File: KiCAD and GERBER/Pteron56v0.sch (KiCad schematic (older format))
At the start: 46 parts, among them J1 AudioJack4, J2 AudioJack4, SW10 SW_PUSH, SW12 SW_PUSH, SW13 SW_PUSH, SW14 SW_PUSH, SW15 SW_PUSH, SW17 SW_PUSH, SW18 SW_PUSH, SW19 SW_PUSH, SW20 SW_PUSH, SW22 SW_PUSH, SW23 SW_PUSH, SW24 SW_PUSH, SW26 SW_PUSH, SW27 SW_PUSH, SW28 SW_PUSH, SW7 SW_PUSH, SW8 SW_PUSH, SW9 SW_PUSH, U1 ProMicro

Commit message: simplified wiring, lily58 like pro micro placement
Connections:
- net Col1: now also U1.17 (F7); no longer U1.13 (B6)
- net Col2: now also U1.16 (B1); no longer U1.15 (B3)
- net Col3: now also U1.15 (B3); no longer U1.16 (B1)
- net Col4: now also U1.14 (B2); no longer U1.18 (F6)
- net Col5: now also U1.13 (B6); no longer U1.17 (F7)
- net Row1: now also U1.10 (E6); no longer U1.9 (D7)
- net Row2: now also U1.9 (D7); no longer U1.10 (E6)
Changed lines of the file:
@@
 Text Label 3350 4000 0    50   ~ 0
 Col4
+Text Label 8100 5450 0    50   ~ 0
+Row1
 Text Label 8100 5350 0    50   ~ 0
-Row1
-Text Label 8100 5450 0    50   ~ 0
 Row2
 Text Label 8100 5550 0    50   ~ 0
@@
 Text Label 8100 5650 0    50   ~ 0
 Row4
-Text Label 10000 5650 0    50   ~ 0
+Text Label 10000 5250 0    50   ~ 0
 Col1
+Text Label 10000 5350 0    50   ~ 0
+Col2
 Text Label 10000 5450 0    50   ~ 0
-Col2
-Text Label 10000 5350 0    50   ~ 0
 Col3
-Text Label 10000 5150 0    50   ~ 0
+Text Label 10000 5550 0    50   ~ 0
 Col4
-Text Label 10000 5250 0    50   ~ 0
-Col5
 Wire Wire Line
 	8100 5650 8400 5650
 Wire Wire Line
-	9800 5150 10000 5150
-Wire Wire Line
 	9800 5250 10000 5250
 Wire Wire Line
 	9800 5350 10000 5350
-Wire Wire Line
-	9800 5450 10000 5450
 Wire Wire Line
 	9800 5650 10000 5650
@@
 	1    0    0    -1
 $EndComp
+Wire Wire Line
+	9800 5550 10000 5550
+Wire Wire Line
+	9800 5450 10000 5450
+Text Label 10000 5650 0    50   ~ 0
+Col5
 $EndSCHEMATC

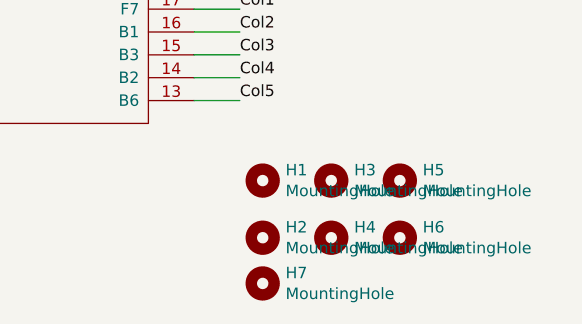
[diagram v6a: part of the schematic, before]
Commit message: made small changes for mounting holes
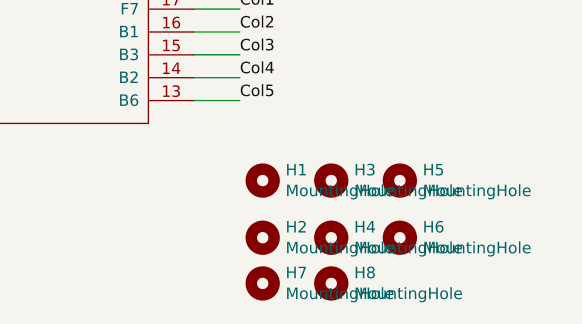
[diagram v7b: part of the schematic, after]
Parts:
- added H8: MountingHole, MountingHole:MountingHole_3.2mm_M3, symbol Mechanical:MountingHole
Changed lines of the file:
@@
 Text Label 10000 5650 0    50   ~ 0
 Col5
+$Comp
+L Mechanical:MountingHole H8
+U 1 1 60793C0F
+P 10400 6450
+F 0 "H8" H 10500 6496 50  0000 L CNN
+F 1 "MountingHole" H 10500 6405 50  0000 L CNN
+F 2 "MountingHole:MountingHole_3.2mm_M3" H 10400 6450 50  0001 C CNN
+F 3 "~" H 10400 6450 50  0001 C CNN
+	1    10400 6450
+	1    0    0    -1
+$EndComp
 $EndSCHEMATC

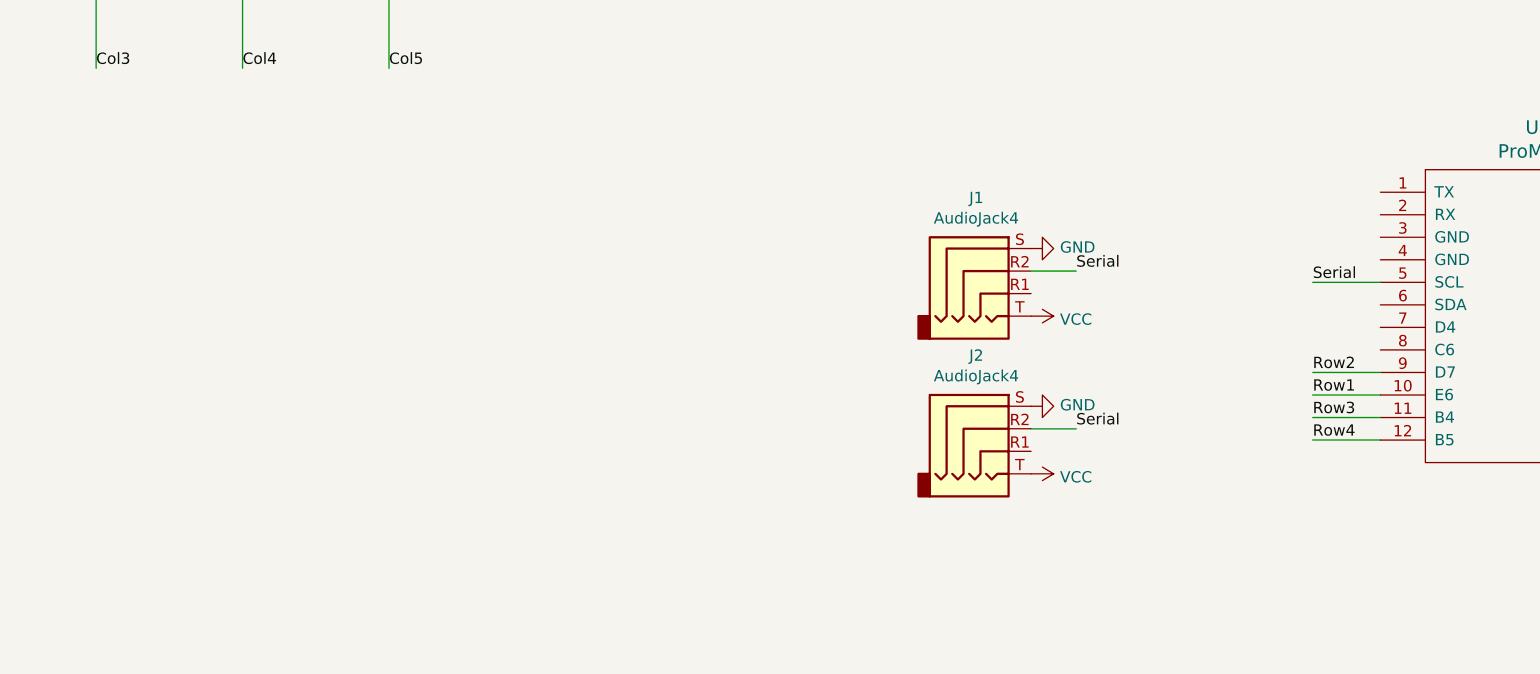
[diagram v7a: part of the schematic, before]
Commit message: added oled support
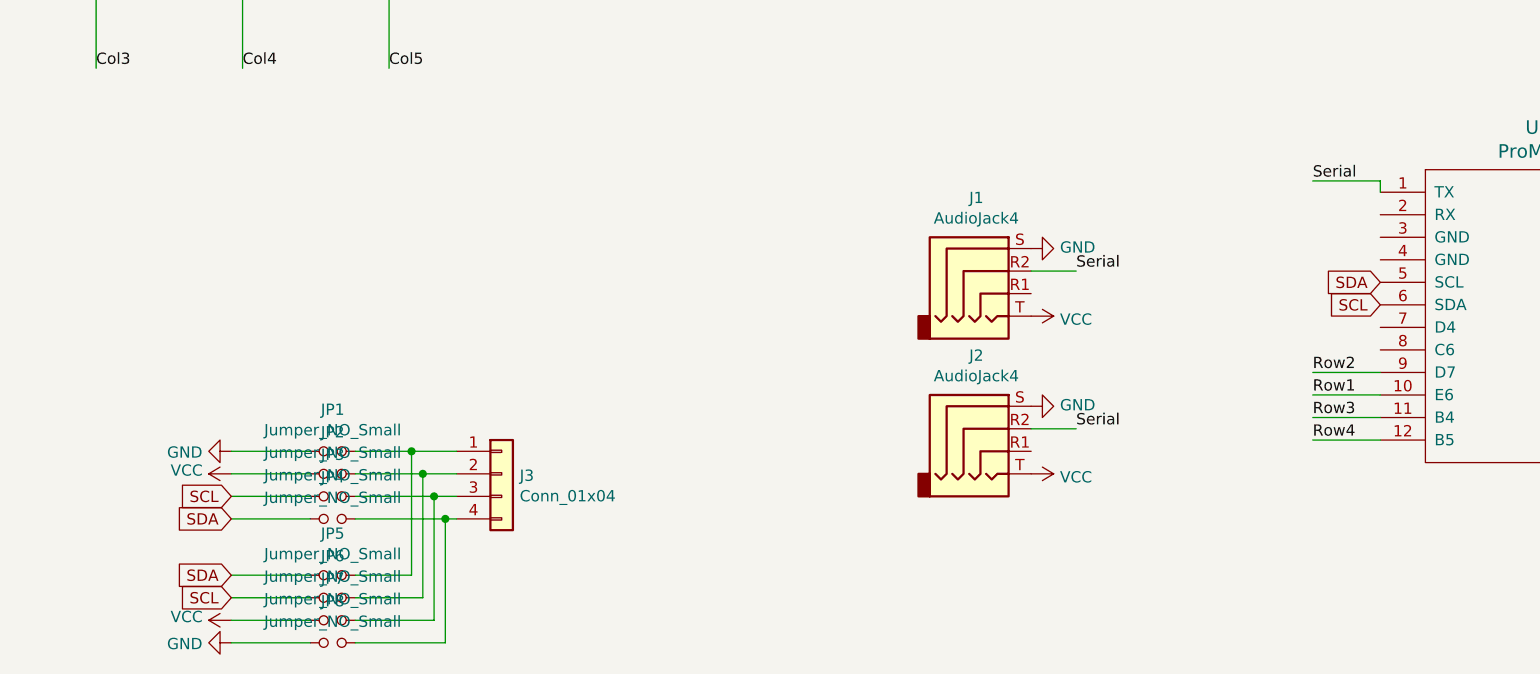
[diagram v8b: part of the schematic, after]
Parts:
- added J3: Conn_01x04, usbc_footprint:OLED_4Pin_outline, symbol Connector_Generic:Conn_01x04
- added JP1, JP2, JP3, JP4, JP5, JP6, JP7, JP8: Jumper_NO_Small, SparkFun-Passives:PAD-JUMPER-2-NO_NO_SILK, symbol Device:Jumper_NO_Small
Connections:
- net GND: now also JP1.1, JP8.1
- net Serial: now also U1.1 (TX); no longer U1.5 (SCL)
- net VCC: now also JP2.1, JP7.1
- net SCL: now reaches U1.6 (SDA)
- net SCL: now also JP3.1, JP6.1
- new net: J3.1 (Pin_1), JP1.2, JP5.2
- new net: J3.2 (Pin_2), JP2.2, JP6.2
- new net: J3.3 (Pin_3), JP3.2, JP7.2
- new net: J3.4 (Pin_4), JP4.2, JP8.2
- new net SDA: JP4.1, JP5.1, U1.5 (SCL)
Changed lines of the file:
@@
 Wire Wire Line
 	8100 5550 8400 5550
-Wire Wire Line
-	8400 4950 8100 4950
-Text Label 8100 4950 0    50   ~ 0
+Text Label 8100 4500 0    50   ~ 0
 Serial
 $Comp
@@
 	1    0    0    -1
 $EndComp
+$Comp
+L Connector_Generic:Conn_01x04 J3
+U 1 1 60775285
+P 4500 5800
+F 0 "J3" H 4580 5792 50  0000 L CNN
+F 1 "Conn_01x04" H 4580 5701 50  0000 L CNN
+F 2 "usbc_footprint:OLED_4Pin_outline" H 4500 5800 50  0001 C CNN
+F 3 "~" H 4500 5800 50  0001 C CNN
+	1    4500 5800
+	1    0    0    -1
+$EndComp
+Wire Wire Line
+	8100 4500 8400 4500
+Wire Wire Line
+	8400 4500 8400 4550
+Wire Wire Line
+	4300 5700 4100 5700
+Wire Wire Line
+	4300 5800 4150 5800
+Wire Wire Line
+	3850 5900 4200 5900
+Wire Wire Line
+	4300 6000 4250 6000
+Wire Wire Line
+	4100 5700 4100 6250
+Wire Wire Line
+	4100 6250 3850 6250
+Connection ~ 4100 5700
+Wire Wire Line
+	4100 5700 3850 5700
+Wire Wire Line
+	4150 5800 4150 6350
+Wire Wire Line
+	4150 6350 3850 6350
+Connection ~ 4150 5800
+Wire Wire Line
+	4150 5800 3850 5800
+Wire Wire Line
+	4200 5900 4200 6450
+Wire Wire Line
+	4200 6450 3850 6450
+Connection ~ 4200 5900
+Wire Wire Line
+	4200 5900 4300 5900
+Wire Wire Line
+	4250 6000 4250 6550
+Wire Wire Line
+	4250 6550 3850 6550
+Connection ~ 4250 6000
+Wire Wire Line
+	4250 6000 3850 6000
+$Comp
+L Device:Jumper_NO_Small JP1
+U 1 1 60791352
+P 3750 5700
+F 0 "JP1" H 3750 5885 50  0000 C CNN
+F 1 "Jumper_NO_Small" H 3750 5794 50  0000 C CNN
+F 2 "SparkFun-Passives:PAD-JUMPER-2-NO_NO_SILK" H 3750 5700 50  0001 C CNN
+F 3 "~" H 3750 5700 50  0001 C CNN
+	1    3750 5700
+	1    0    0    -1
+$EndComp
+$Comp
+L Device:Jumper_NO_Small JP2
+U 1 1 607919BE
+P 3750 5800
+F 0 "JP2" H 3750 5985 50  0000 C CNN
+F 1 "Jumper_NO_Small" H 3750 5894 50  0000 C CNN
+F 2 "SparkFun-Passives:PAD-JUMPER-2-NO_NO_SILK" H 3750 5800 50  0001 C CNN
+F 3 "~" H 3750 5800 50  0001 C CNN
+	1    3750 5800
+	1    0    0    -1
+$EndComp
+$Comp
+L Device:Jumper_NO_Small JP3
+U 1 1 60791C36
+P 3750 5900
+F 0 "JP3" H 3750 6085 50  0000 C CNN
+F 1 "Jumper_NO_Small" H 3750 5994 50  0000 C CNN
+F 2 "SparkFun-Passives:PAD-JUMPER-2-NO_NO_SILK" H 3750 5900 50  0001 C CNN
+F 3 "~" H 3750 5900 50  0001 C CNN
+	1    3750 5900
+	1    0    0    -1
+$EndComp
+$Comp
+L Device:Jumper_NO_Small JP4
+U 1 1 60791EC7
+P 3750 6000
+F 0 "JP4" H 3750 6185 50  0000 C CNN
+F 1 "Jumper_NO_Small" H 3750 6094 50  0000 C CNN
+F 2 "SparkFun-Passives:PAD-JUMPER-2-NO_NO_SILK" H 3750 6000 50  0001 C CNN
+F 3 "~" H 3750 6000 50  0001 C CNN
+	1    3750 6000
+	1    0    0    -1
+$EndComp
+$Comp
+L Device:Jumper_NO_Small JP5
+U 1 1 60792104
+P 3750 6250
+F 0 "JP5" H 3750 6435 50  0000 C CNN
+F 1 "Jumper_NO_Small" H 3750 6344 50  0000 C CNN
+F 2 "SparkFun-Passives:PAD-JUMPER-2-NO_NO_SILK" H 3750 6250 50  0001 C CNN
+F 3 "~" H 3750 6250 50  0001 C CNN
+	1    3750 6250
+	1    0    0    -1
+$EndComp
+$Comp
+L Device:Jumper_NO_Small JP6
+U 1 1 607923D2
+P 3750 6350
+F 0 "JP6" H 3750 6535 50  0000 C CNN
+F 1 "Jumper_NO_Small" H 3750 6444 50  0000 C CNN
+F 2 "SparkFun-Passives:PAD-JUMPER-2-NO_NO_SILK" H 3750 6350 50  0001 C CNN
+F 3 "~" H 3750 6350 50  0001 C CNN
+	1    3750 6350
+	1    0    0    -1
+$EndComp
+$Comp
+L Device:Jumper_NO_Small JP7
+U 1 1 6079263D
+P 3750 6450
+F 0 "JP7" H 3750 6635 50  0000 C CNN
+F 1 "Jumper_NO_Small" H 3750 6544 50  0000 C CNN
+F 2 "SparkFun-Passives:PAD-JUMPER-2-NO_NO_SILK" H 3750 6450 50  0001 C CNN
+F 3 "~" H 3750 6450 50  0001 C CNN
+	1    3750 6450
+	1    0    0    -1
+$EndComp
+$Comp
+L Device:Jumper_NO_Small JP8
+U 1 1 6079280A
+P 3750 6550
+F 0 "JP8" H 3750 6735 50  0000 C CNN
+F 1 "Jumper_NO_Small" H 3750 6644 50  0000 C CNN
+F 2 "SparkFun-Passives:PAD-JUMPER-2-NO_NO_SILK" H 3750 6550 50  0001 C CNN
+F 3 "~" H 3750 6550 50  0001 C CNN
+	1    3750 6550
+	1    0    0    -1
+$EndComp
+Wire Wire Line
+	3650 6000 3300 6000
+Wire Wire Line
+	3650 5900 3300 5900
+Wire Wire Line
+	3650 5800 3300 5800
+Wire Wire Line
+	3650 5700 3300 5700
+Wire Wire Line
+	3650 6250 3300 6250
+Wire Wire Line
+	3650 6350 3300 6350
+Wire Wire Line
+	3650 6450 3300 6450
+Wire Wire Line
+	3650 6550 3300 6550
+Text GLabel 3300 6000 0    50   Input ~ 0
+SDA
+Text GLabel 3300 5900 0    50   Input ~ 0
+SCL
+$Comp
+L power:VCC #PWR0105
+U 1 1 607B52AE
+P 3300 5800
+F 0 "#PWR0105" H 3300 5650 50  0001 C CNN
+F 1 "VCC" V 3315 5927 50  0000 L CNN
+F 2 "" H 3300 5800 50  0001 C CNN
+F 3 "" H 3300 5800 50  0001 C CNN
+	1    3300 5800
+	0    -1   -1   0
+$EndComp
+$Comp
+L power:GND #PWR0106
+U 1 1 607B5F3E
+P 3300 5700
+F 0 "#PWR0106" H 3300 5450 50  0001 C CNN
+F 1 "GND" V 3305 5572 50  0000 R CNN
+F 2 "" H 3300 5700 50  0001 C CNN
+F 3 "" H 3300 5700 50  0001 C CNN
+	1    3300 5700
+	0    1    1    0
+$EndComp
+Text GLabel 3300 6250 0    50   Input ~ 0
+SDA
+Text GLabel 3300 6350 0    50   Input ~ 0
+SCL
+$Comp
+L power:VCC #PWR0107
+U 1 1 607B6A8D
+P 3300 6450
+F 0 "#PWR0107" H 3300 6300 50  0001 C CNN
+F 1 "VCC" V 3315 6577 50  0000 L CNN
+F 2 "" H 3300 6450 50  0001 C CNN
+F 3 "" H 3300 6450 50  0001 C CNN
+	1    3300 6450
+	0    -1   -1   0
+$EndComp
+$Comp
+L power:GND #PWR0108
+U 1 1 607B6FB5
+P 3300 6550
+F 0 "#PWR0108" H 3300 6300 50  0001 C CNN
+F 1 "GND" V 3305 6422 50  0000 R CNN
+F 2 "" H 3300 6550 50  0001 C CNN
+F 3 "" H 3300 6550 50  0001 C CNN
+	1    3300 6550
+	0    1    1    0
+$EndComp
+Text GLabel 8400 4950 0    50   Input ~ 0
+SDA
+Text GLabel 8400 5050 0    50   Input ~ 0
+SCL
 $EndSCHEMATC
